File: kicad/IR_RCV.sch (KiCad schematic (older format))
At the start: 19 parts, among them P10 Partition, P5 PR_Host, P6 PR_Slave, P7 Partition, P8 Partition, P9 Partition, Q1 IRFML8244, U6 AD8601

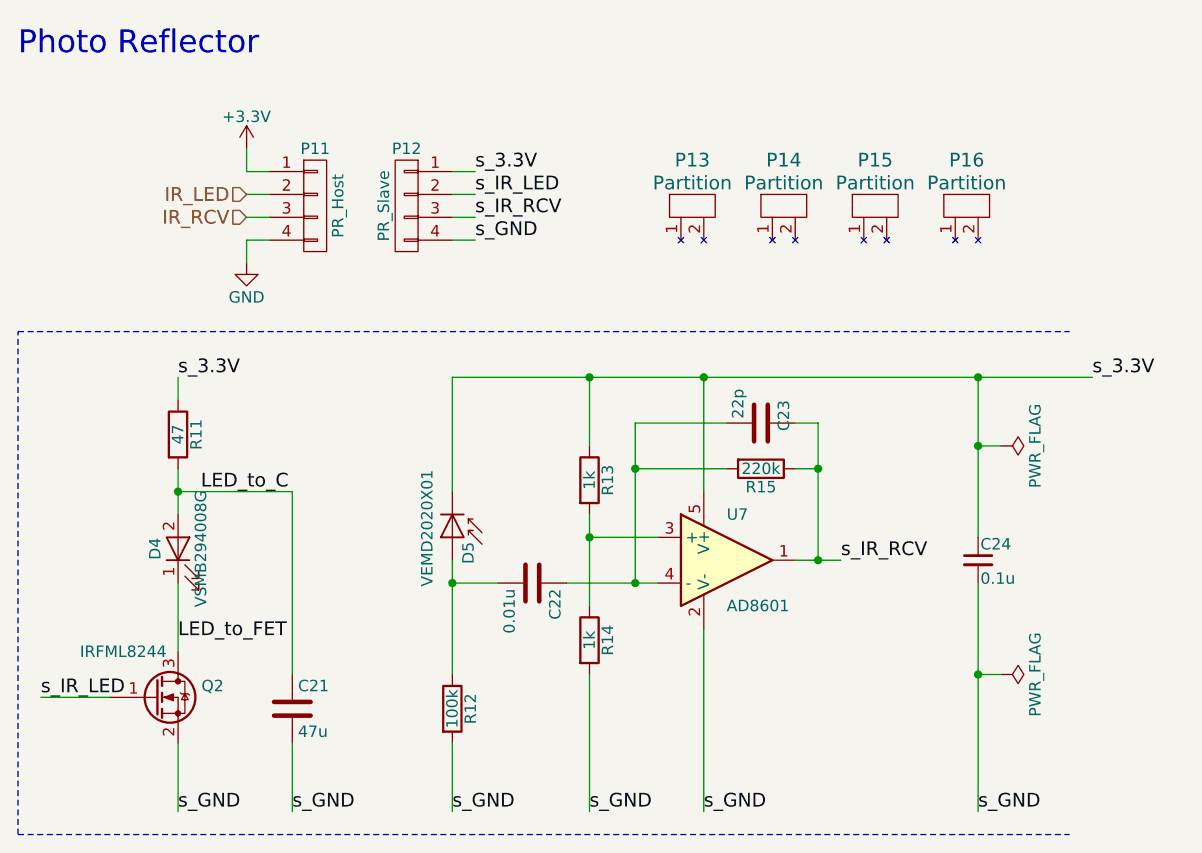
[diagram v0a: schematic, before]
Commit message: 4輪の改良版を設計
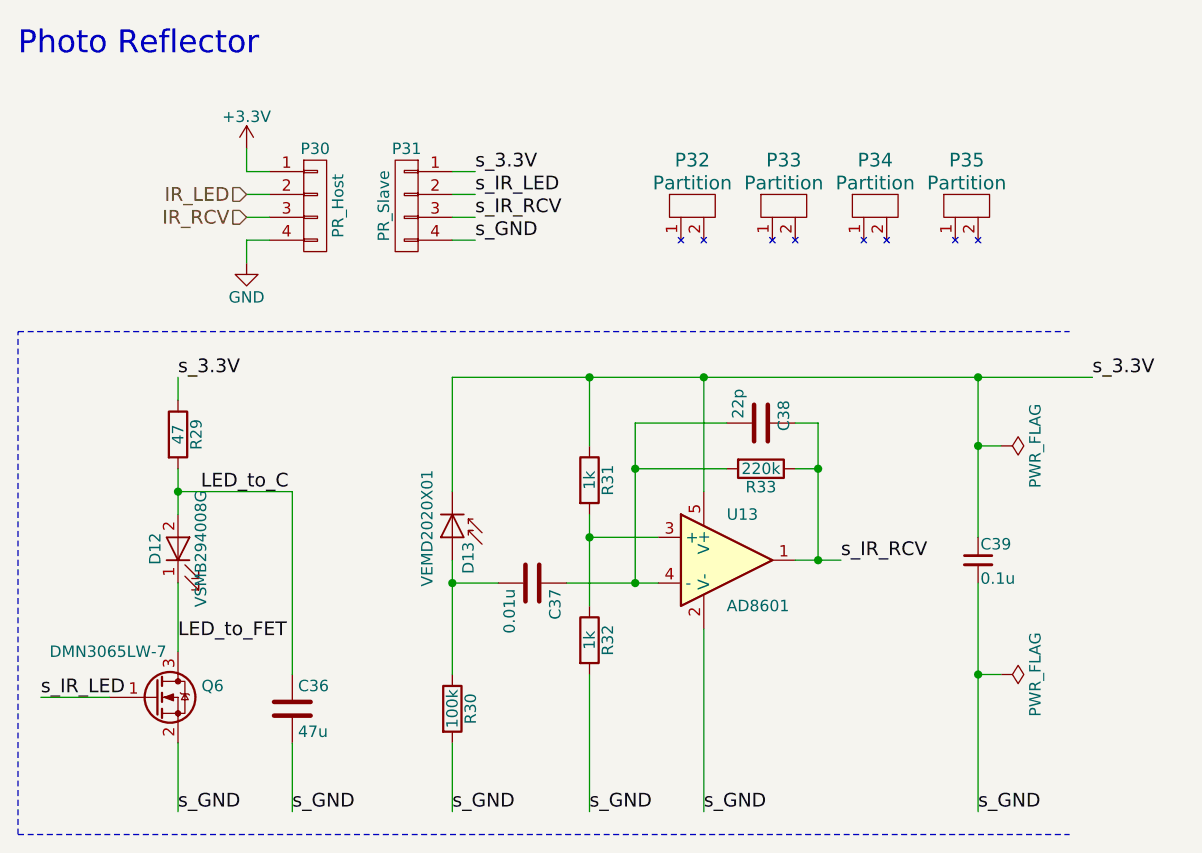
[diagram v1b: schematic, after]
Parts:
- P10: footprint mouse:Partition_Slave -> mouse:Partition_long_Slave
- P9: footprint mouse:Partition_Host -> mouse:Partition_Long_Host
- Q1: value IRFML8244 -> DMN3065LW-7; footprint TO_SOT_Packages_SMD:SOT-23 -> TO_SOT_Packages_SMD:SOT-323_SC-70
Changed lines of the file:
@@
 LIBS:zetex
 LIBS:Zilog
-LIBS:KERISE-cache
 EELAYER 25 0
 EELAYER END
 $Descr A4 11693 8268
 encoding utf-8
-Sheet 5 13
+Sheet 4 14
 Title ""
 Date ""
@@
 AR Path="/57CF0B09/589BE652" Ref="P6"  Part="1"
 AR Path="/57CF2A30/589BE652" Ref="P12"  Part="1"
-F 0 "P12" H 5400 2800 50  0000 C CNN
+AR Path="/597E1B35/589BE652" Ref="P25"  Part="1"
+AR Path="/597E1B39/589BE652" Ref="P31"  Part="1"
+F 0 "P31" H 5400 2800 50  0000 C CNN
 F 1 "PR_Slave" V 5500 2550 50  0000 C CNN
 F 2 "mouse:STAND_PR_SLAVE" H 5400 2550 50  0001 C CNN
@@
 AR Path="/57CF0B09/589BE75A" Ref="Q1"  Part="1"
 AR Path="/57CF2A30/589BE75A" Ref="Q2"  Part="1"
-F 0 "Q2" H 4600 4750 50  0000 R CNN
-F 1 "IRFML8244" H 4350 4900 50  0000 R CNN
-F 2 "TO_SOT_Packages_SMD:SOT-23" H 4500 4800 50  0001 C CNN
+AR Path="/597E1B35/589BE75A" Ref="Q5"  Part="1"
+AR Path="/597E1B39/589BE75A" Ref="Q6"  Part="1"
+F 0 "Q6" H 4600 4750 50  0000 R CNN
+F 1 "DMN3065LW-7" H 4350 4900 50  0000 R CNN
+F 2 "TO_SOT_Packages_SMD:SOT-323_SC-70" H 4500 4800 50  0001 C CNN
 F 3 "" H 4300 4700 50  0000 C CNN
 	1    4300 4700
@@
 AR Path="/57CF0B09/589BE76D" Ref="R6"  Part="1"
 AR Path="/57CF2A30/589BE76D" Ref="R11"  Part="1"
-F 0 "R11" V 4480 3550 50  0000 C CNN
+AR Path="/597E1B35/589BE76D" Ref="R24"  Part="1"
+AR Path="/597E1B39/589BE76D" Ref="R29"  Part="1"
+F 0 "R29" V 4480 3550 50  0000 C CNN
 F 1 "47" V 4400 3550 50  0000 C CNN
 F 2 "Resistors_SMD:R_0603" V 4330 3550 50  0001 C CNN
@@
 AR Path="/57CF0B09/589BE88F" Ref="P5"  Part="1"
 AR Path="/57CF2A30/589BE88F" Ref="P11"  Part="1"
-F 0 "P11" H 5000 2800 50  0000 C CNN
+AR Path="/597E1B35/589BE88F" Ref="P24"  Part="1"
+AR Path="/597E1B39/589BE88F" Ref="P30"  Part="1"
+F 0 "P30" H 5000 2800 50  0000 C CNN
 F 1 "PR_Host" V 5100 2550 50  0000 C CNN
 F 2 "mouse:STAND_PR_HOST" H 5000 2550 50  0001 C CNN
@@
 AR Path="/57CF0B09/589BEE3B" Ref="R7"  Part="1"
 AR Path="/57CF2A30/589BEE3B" Ref="R12"  Part="1"
-F 0 "R12" V 5680 4750 50  0000 C CNN
+AR Path="/597E1B35/589BEE3B" Ref="R25"  Part="1"
+AR Path="/597E1B39/589BEE3B" Ref="R30"  Part="1"
+F 0 "R30" V 5680 4750 50  0000 C CNN
 F 1 "100k" V 5600 4750 50  0000 C CNN
 F 2 "Resistors_SMD:R_0201" V 5530 4750 50  0001 C CNN
@@
 AR Path="/57CF0B09/589BF265" Ref="#PWR038"  Part="1"
 AR Path="/57CF2A30/589BF265" Ref="#PWR042"  Part="1"
-F 0 "#PWR042" H 4700 2550 50  0001 C CNN
+AR Path="/597E1B35/589BF265" Ref="#PWR074"  Part="1"
+AR Path="/597E1B39/589BF265" Ref="#PWR078"  Part="1"
+F 0 "#PWR078" H 4700 2550 50  0001 C CNN
 F 1 "GND" H 4700 2650 50  0000 C CNN
 F 2 "" H 4700 2800 50  0000 C CNN
@@
 AR Path="/57CF0B09/589EE263" Ref="C17"  Part="1"
 AR Path="/57CF2A30/589EE263" Ref="C21"  Part="1"
-F 0 "C21" H 4925 4850 50  0000 L CNN
+AR Path="/597E1B35/589EE263" Ref="C32"  Part="1"
+AR Path="/597E1B39/589EE263" Ref="C36"  Part="1"
+F 0 "C36" H 4925 4850 50  0000 L CNN
 F 1 "47u" H 4925 4650 50  0000 L CNN
 F 2 "Capacitors_SMD:C_0805" H 4938 4600 50  0001 C CNN
@@
 AR Path="/57CF0B09/589CC209" Ref="#PWR039"  Part="1"
 AR Path="/57CF2A30/589CC209" Ref="#PWR043"  Part="1"
-F 0 "#PWR043" H 4700 2150 50  0001 C CNN
+AR Path="/597E1B35/589CC209" Ref="#PWR075"  Part="1"
+AR Path="/597E1B39/589CC209" Ref="#PWR079"  Part="1"
+F 0 "#PWR079" H 4700 2150 50  0001 C CNN
 F 1 "+3.3V" H 4700 2440 50  0000 C CNN
 F 2 "" H 4700 2300 50  0000 C CNN
@@
 AR Path="/57CF0B09/58A0483E" Ref="R8"  Part="1"
 AR Path="/57CF2A30/58A0483E" Ref="R13"  Part="1"
-F 0 "R13" V 6280 3750 50  0000 C CNN
+AR Path="/597E1B35/58A0483E" Ref="R26"  Part="1"
+AR Path="/597E1B39/58A0483E" Ref="R31"  Part="1"
+F 0 "R31" V 6280 3750 50  0000 C CNN
 F 1 "1k" V 6200 3750 50  0000 C CNN
 F 2 "Resistors_SMD:R_0201" V 6130 3750 50  0001 C CNN
@@
 AR Path="/57CF0B09/57CF0F5E" Ref="C19"  Part="1"
 AR Path="/57CF2A30/57CF0F5E" Ref="C23"  Part="1"
-F 0 "C23" H 6850 3600 50  0000 L CNN
+AR Path="/597E1B35/57CF0F5E" Ref="C34"  Part="1"
+AR Path="/597E1B39/57CF0F5E" Ref="C38"  Part="1"
+F 0 "C38" H 6850 3600 50  0000 L CNN
 F 1 "22p" H 6800 3400 50  0000 L CNN
 F 2 "Capacitors_SMD:C_0201" H 6988 3350 50  0001 C CNN
@@
 AR Path="/57CF0B09/57CF0F57" Ref="R10"  Part="1"
 AR Path="/57CF2A30/57CF0F57" Ref="R15"  Part="1"
-F 0 "R15" V 7030 3700 50  0000 C CNN
+AR Path="/597E1B35/57CF0F57" Ref="R28"  Part="1"
+AR Path="/597E1B39/57CF0F57" Ref="R33"  Part="1"
+F 0 "R33" V 7030 3700 50  0000 C CNN
 F 1 "220k" V 6950 3700 50  0000 C CNN
 F 2 "Resistors_SMD:R_0201" V 6880 3700 50  0001 C CNN
@@
 AR Path="/57CF0B09/5925867D" Ref="C20"  Part="1"
 AR Path="/57CF2A30/5925867D" Ref="C24"  Part="1"
-F 0 "C24" H 7910 4170 50  0000 L CNN
+AR Path="/597E1B35/5925867D" Ref="C35"  Part="1"
+AR Path="/597E1B39/5925867D" Ref="C39"  Part="1"
+F 0 "C39" H 7910 4170 50  0000 L CNN
 F 1 "0.1u" H 7910 4020 50  0000 L CNN
 F 2 "Capacitors_SMD:C_0201" H 7900 4100 50  0001 C CNN
@@
 AR Path="/57CF0B09/58A04889" Ref="R9"  Part="1"
 AR Path="/57CF2A30/58A04889" Ref="R14"  Part="1"
-F 0 "R14" V 6280 4450 50  0000 C CNN
+AR Path="/597E1B35/58A04889" Ref="R27"  Part="1"
+AR Path="/597E1B39/58A04889" Ref="R32"  Part="1"
+F 0 "R32" V 6280 4450 50  0000 C CNN
 F 1 "1k" V 6200 4450 50  0000 C CNN
 F 2 "Resistors_SMD:R_0201" V 6130 4450 50  0001 C CNN
@@
 AR Path="/57CF0B09/57CF0F45" Ref="C18"  Part="1"
 AR Path="/57CF2A30/57CF0F45" Ref="C22"  Part="1"
-F 0 "C22" H 5975 4300 50  0000 L CNN
+AR Path="/597E1B35/57CF0F45" Ref="C33"  Part="1"
+AR Path="/597E1B39/57CF0F45" Ref="C37"  Part="1"
+F 0 "C37" H 5975 4300 50  0000 L CNN
 F 1 "0.01u" H 5975 4100 50  0000 L CNN
 F 2 "Capacitors_SMD:C_0201" H 5988 4050 50  0001 C CNN
@@
 AR Path="/57CF0B09/59497B18" Ref="P7"  Part="1"
 AR Path="/57CF2A30/59497B18" Ref="P13"  Part="1"
-F 0 "P13" H 6650 2550 60  0000 C CNN
+AR Path="/597E1B35/59497B18" Ref="P26"  Part="1"
+AR Path="/597E1B39/59497B18" Ref="P32"  Part="1"
+F 0 "P32" H 6650 2550 60  0000 C CNN
 F 1 "Partition" H 6650 2450 60  0000 C CNN
 F 2 "mouse:Partition_Host" H 6650 2450 60  0001 C CNN
@@
 AR Path="/57CF0B09/59497CA2" Ref="P8"  Part="1"
 AR Path="/57CF2A30/59497CA2" Ref="P14"  Part="1"
-F 0 "P14" H 7050 2550 60  0000 C CNN
+AR Path="/597E1B35/59497CA2" Ref="P27"  Part="1"
+AR Path="/597E1B39/59497CA2" Ref="P33"  Part="1"
+F 0 "P33" H 7050 2550 60  0000 C CNN
 F 1 "Partition" H 7050 2450 60  0000 C CNN
 F 2 "mouse:Partition_Slave" H 7050 2450 60  0001 C CNN
@@
 AR Path="/57CF0B09/59497CF1" Ref="P9"  Part="1"
 AR Path="/57CF2A30/59497CF1" Ref="P15"  Part="1"
-F 0 "P15" H 7450 2550 60  0000 C CNN
+AR Path="/597E1B35/59497CF1" Ref="P28"  Part="1"
+AR Path="/597E1B39/59497CF1" Ref="P34"  Part="1"
+F 0 "P34" H 7450 2550 60  0000 C CNN
 F 1 "Partition" H 7450 2450 60  0000 C CNN
-F 2 "mouse:Partition_Host" H 7450 2450 60  0001 C CNN
+F 2 "mouse:Partition_Long_Host" H 7450 2450 60  0001 C CNN
 F 3 "" H 7450 2450 60  0001 C CNN
 	1    7450 2450
@@
 AR Path="/57CF0B09/59497D43" Ref="P10"  Part="1"
 AR Path="/57CF2A30/59497D43" Ref="P16"  Part="1"
-F 0 "P16" H 7850 2550 60  0000 C CNN
+AR Path="/597E1B35/59497D43" Ref="P29"  Part="1"
+AR Path="/597E1B39/59497D43" Ref="P35"  Part="1"
+F 0 "P35" H 7850 2550 60  0000 C CNN
 F 1 "Partition" H 7850 2450 60  0000 C CNN
-F 2 "mouse:Partition_Slave" H 7850 2450 60  0001 C CNN
+F 2 "mouse:Partition_long_Slave" H 7850 2450 60  0001 C CNN
 F 3 "" H 7850 2450 60  0001 C CNN
 	1    7850 2450
@@
 AR Path="/57CF0B09/594AC13D" Ref="U6"  Part="1"
 AR Path="/57CF2A30/594AC13D" Ref="U7"  Part="1"
-F 0 "U7" H 6800 4300 50  0000 L CNN
+AR Path="/597E1B35/594AC13D" Ref="U12"  Part="1"
+AR Path="/597E1B39/594AC13D" Ref="U13"  Part="1"
+F 0 "U13" H 6800 4300 50  0000 L CNN
 F 1 "AD8601" H 6800 3900 50  0000 L CNN
 F 2 "TO_SOT_Packages_SMD:SOT-23-5" H 6800 3700 50  0001 C CNN
@@
 AR Path="/57CF0B09/594AC36C" Ref="D3"  Part="1"
 AR Path="/57CF2A30/594AC36C" Ref="D5"  Part="1"
-F 0 "D5" H 5620 4070 50  0000 L CNN
+AR Path="/597E1B35/594AC36C" Ref="D11"  Part="1"
+AR Path="/597E1B39/594AC36C" Ref="D13"  Part="1"
+F 0 "D13" H 5620 4070 50  0000 L CNN
 F 1 "VEMD2020X01" H 5560 3890 50  0000 C CNN
 F 2 "mouse:VISHAY_DIODE" H 5550 4000 50  0001 C CNN
@@
 AR Path="/57CF0B09/594AC674" Ref="D2"  Part="1"
 AR Path="/57CF2A30/594AC674" Ref="D4"  Part="1"
-F 0 "D4" H 4400 4150 50  0000 C CNN
+AR Path="/597E1B35/594AC674" Ref="D10"  Part="1"
+AR Path="/597E1B39/594AC674" Ref="D12"  Part="1"
+F 0 "D12" H 4400 4150 50  0000 C CNN
 F 1 "VSMB294008G" H 4400 3950 50  0000 C CNN
 F 2 "mouse:VISHAY_DIODE" H 4400 4050 50  0001 C CNN
@@
 AR Path="/57CF0B09/594B7401" Ref="#FLG040"  Part="1"
 AR Path="/57CF2A30/594B7401" Ref="#FLG044"  Part="1"
-F 0 "#FLG044" H 8000 3675 50  0001 C CNN
+AR Path="/597E1B35/594B7401" Ref="#FLG076"  Part="1"
+AR Path="/597E1B39/594B7401" Ref="#FLG080"  Part="1"
+F 0 "#FLG080" H 8000 3675 50  0001 C CNN
 F 1 "PWR_FLAG" H 8000 3750 50  0000 C CNN
 F 2 "" H 8000 3600 50  0001 C CNN
@@
 AR Path="/57CF0B09/594B744C" Ref="#FLG041"  Part="1"
 AR Path="/57CF2A30/594B744C" Ref="#FLG045"  Part="1"
-F 0 "#FLG045" H 8000 4675 50  0001 C CNN
+AR Path="/597E1B35/594B744C" Ref="#FLG077"  Part="1"
+AR Path="/597E1B39/594B744C" Ref="#FLG081"  Part="1"
+F 0 "#FLG081" H 8000 4675 50  0001 C CNN
 F 1 "PWR_FLAG" H 8000 4750 50  0000 C CNN
 F 2 "" H 8000 4600 50  0001 C CNN

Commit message: 部品を配置
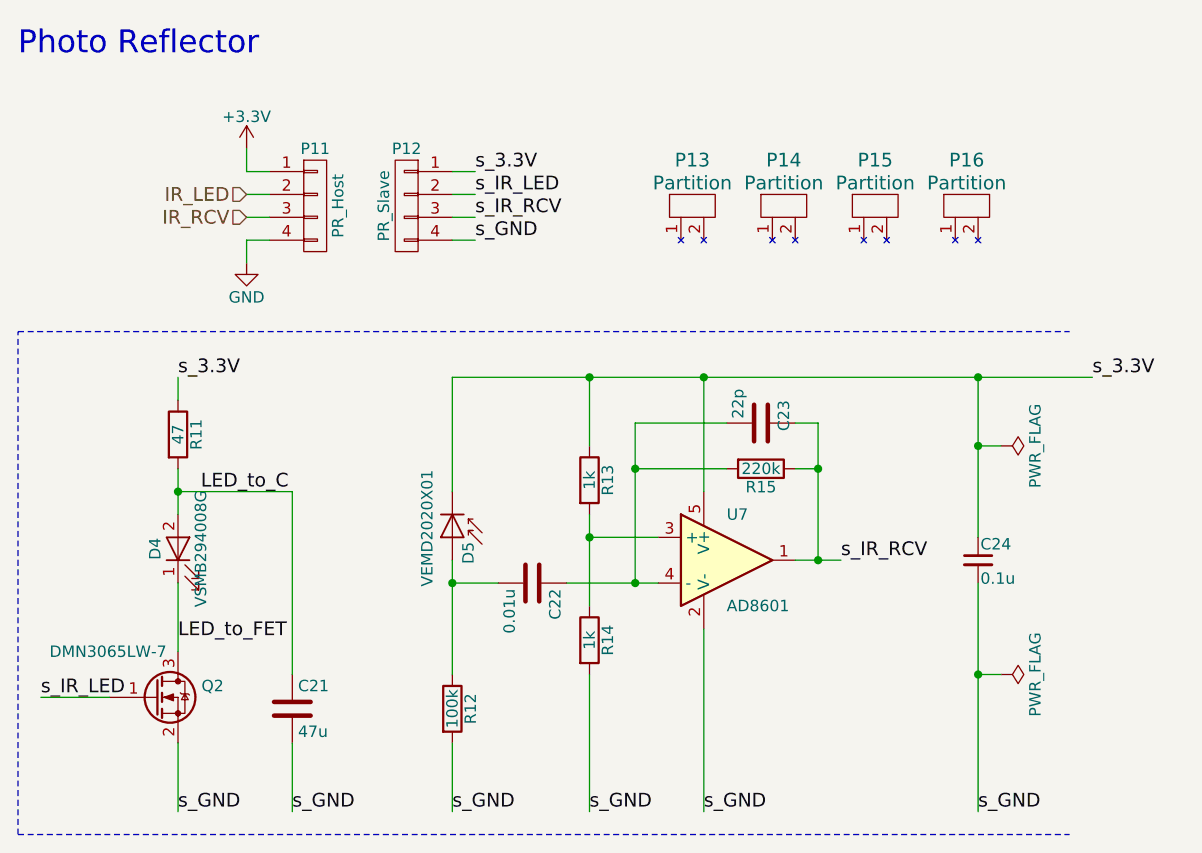
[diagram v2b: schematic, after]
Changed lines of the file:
@@
 AR Path="/597E1B35/589BE652" Ref="P25"  Part="1"
 AR Path="/597E1B39/589BE652" Ref="P31"  Part="1"
-F 0 "P31" H 5400 2800 50  0000 C CNN
+F 0 "P12" H 5400 2800 50  0000 C CNN
 F 1 "PR_Slave" V 5500 2550 50  0000 C CNN
 F 2 "mouse:STAND_PR_SLAVE" H 5400 2550 50  0001 C CNN
@@
 AR Path="/597E1B35/589BE75A" Ref="Q5"  Part="1"
 AR Path="/597E1B39/589BE75A" Ref="Q6"  Part="1"
-F 0 "Q6" H 4600 4750 50  0000 R CNN
+F 0 "Q2" H 4600 4750 50  0000 R CNN
 F 1 "DMN3065LW-7" H 4350 4900 50  0000 R CNN
 F 2 "TO_SOT_Packages_SMD:SOT-323_SC-70" H 4500 4800 50  0001 C CNN
@@
 AR Path="/597E1B35/589BE76D" Ref="R24"  Part="1"
 AR Path="/597E1B39/589BE76D" Ref="R29"  Part="1"
-F 0 "R29" V 4480 3550 50  0000 C CNN
+F 0 "R11" V 4480 3550 50  0000 C CNN
 F 1 "47" V 4400 3550 50  0000 C CNN
 F 2 "Resistors_SMD:R_0603" V 4330 3550 50  0001 C CNN
@@
 AR Path="/597E1B35/589BE88F" Ref="P24"  Part="1"
 AR Path="/597E1B39/589BE88F" Ref="P30"  Part="1"
-F 0 "P30" H 5000 2800 50  0000 C CNN
+F 0 "P11" H 5000 2800 50  0000 C CNN
 F 1 "PR_Host" V 5100 2550 50  0000 C CNN
 F 2 "mouse:STAND_PR_HOST" H 5000 2550 50  0001 C CNN
@@
 AR Path="/597E1B35/589BEE3B" Ref="R25"  Part="1"
 AR Path="/597E1B39/589BEE3B" Ref="R30"  Part="1"
-F 0 "R30" V 5680 4750 50  0000 C CNN
+F 0 "R12" V 5680 4750 50  0000 C CNN
 F 1 "100k" V 5600 4750 50  0000 C CNN
 F 2 "Resistors_SMD:R_0201" V 5530 4750 50  0001 C CNN
@@
 AR Path="/597E1B35/589EE263" Ref="C32"  Part="1"
 AR Path="/597E1B39/589EE263" Ref="C36"  Part="1"
-F 0 "C36" H 4925 4850 50  0000 L CNN
+F 0 "C21" H 4925 4850 50  0000 L CNN
 F 1 "47u" H 4925 4650 50  0000 L CNN
 F 2 "Capacitors_SMD:C_0805" H 4938 4600 50  0001 C CNN
@@
 AR Path="/597E1B35/58A0483E" Ref="R26"  Part="1"
 AR Path="/597E1B39/58A0483E" Ref="R31"  Part="1"
-F 0 "R31" V 6280 3750 50  0000 C CNN
+F 0 "R13" V 6280 3750 50  0000 C CNN
 F 1 "1k" V 6200 3750 50  0000 C CNN
 F 2 "Resistors_SMD:R_0201" V 6130 3750 50  0001 C CNN
@@
 AR Path="/597E1B35/57CF0F5E" Ref="C34"  Part="1"
 AR Path="/597E1B39/57CF0F5E" Ref="C38"  Part="1"
-F 0 "C38" H 6850 3600 50  0000 L CNN
+F 0 "C23" H 6850 3600 50  0000 L CNN
 F 1 "22p" H 6800 3400 50  0000 L CNN
 F 2 "Capacitors_SMD:C_0201" H 6988 3350 50  0001 C CNN
@@
 AR Path="/597E1B35/57CF0F57" Ref="R28"  Part="1"
 AR Path="/597E1B39/57CF0F57" Ref="R33"  Part="1"
-F 0 "R33" V 7030 3700 50  0000 C CNN
+F 0 "R15" V 7030 3700 50  0000 C CNN
 F 1 "220k" V 6950 3700 50  0000 C CNN
 F 2 "Resistors_SMD:R_0201" V 6880 3700 50  0001 C CNN
@@
 AR Path="/597E1B35/5925867D" Ref="C35"  Part="1"
 AR Path="/597E1B39/5925867D" Ref="C39"  Part="1"
-F 0 "C39" H 7910 4170 50  0000 L CNN
+F 0 "C24" H 7910 4170 50  0000 L CNN
 F 1 "0.1u" H 7910 4020 50  0000 L CNN
 F 2 "Capacitors_SMD:C_0201" H 7900 4100 50  0001 C CNN
@@
 AR Path="/597E1B35/58A04889" Ref="R27"  Part="1"
 AR Path="/597E1B39/58A04889" Ref="R32"  Part="1"
-F 0 "R32" V 6280 4450 50  0000 C CNN
+F 0 "R14" V 6280 4450 50  0000 C CNN
 F 1 "1k" V 6200 4450 50  0000 C CNN
 F 2 "Resistors_SMD:R_0201" V 6130 4450 50  0001 C CNN
@@
 AR Path="/597E1B35/57CF0F45" Ref="C33"  Part="1"
 AR Path="/597E1B39/57CF0F45" Ref="C37"  Part="1"
-F 0 "C37" H 5975 4300 50  0000 L CNN
+F 0 "C22" H 5975 4300 50  0000 L CNN
 F 1 "0.01u" H 5975 4100 50  0000 L CNN
 F 2 "Capacitors_SMD:C_0201" H 5988 4050 50  0001 C CNN
@@
 AR Path="/597E1B35/59497B18" Ref="P26"  Part="1"
 AR Path="/597E1B39/59497B18" Ref="P32"  Part="1"
-F 0 "P32" H 6650 2550 60  0000 C CNN
+F 0 "P13" H 6650 2550 60  0000 C CNN
 F 1 "Partition" H 6650 2450 60  0000 C CNN
 F 2 "mouse:Partition_Host" H 6650 2450 60  0001 C CNN
@@
 AR Path="/597E1B35/59497CA2" Ref="P27"  Part="1"
 AR Path="/597E1B39/59497CA2" Ref="P33"  Part="1"
-F 0 "P33" H 7050 2550 60  0000 C CNN
+F 0 "P14" H 7050 2550 60  0000 C CNN
 F 1 "Partition" H 7050 2450 60  0000 C CNN
 F 2 "mouse:Partition_Slave" H 7050 2450 60  0001 C CNN
@@
 AR Path="/597E1B35/59497CF1" Ref="P28"  Part="1"
 AR Path="/597E1B39/59497CF1" Ref="P34"  Part="1"
-F 0 "P34" H 7450 2550 60  0000 C CNN
+F 0 "P15" H 7450 2550 60  0000 C CNN
 F 1 "Partition" H 7450 2450 60  0000 C CNN
 F 2 "mouse:Partition_Long_Host" H 7450 2450 60  0001 C CNN
@@
 AR Path="/597E1B35/59497D43" Ref="P29"  Part="1"
 AR Path="/597E1B39/59497D43" Ref="P35"  Part="1"
-F 0 "P35" H 7850 2550 60  0000 C CNN
+F 0 "P16" H 7850 2550 60  0000 C CNN
 F 1 "Partition" H 7850 2450 60  0000 C CNN
 F 2 "mouse:Partition_long_Slave" H 7850 2450 60  0001 C CNN
@@
 AR Path="/597E1B35/594AC13D" Ref="U12"  Part="1"
 AR Path="/597E1B39/594AC13D" Ref="U13"  Part="1"
-F 0 "U13" H 6800 4300 50  0000 L CNN
+F 0 "U7" H 6800 4300 50  0000 L CNN
 F 1 "AD8601" H 6800 3900 50  0000 L CNN
 F 2 "TO_SOT_Packages_SMD:SOT-23-5" H 6800 3700 50  0001 C CNN
@@
 AR Path="/597E1B35/594AC36C" Ref="D11"  Part="1"
 AR Path="/597E1B39/594AC36C" Ref="D13"  Part="1"
-F 0 "D13" H 5620 4070 50  0000 L CNN
+F 0 "D5" H 5620 4070 50  0000 L CNN
 F 1 "VEMD2020X01" H 5560 3890 50  0000 C CNN
 F 2 "mouse:VISHAY_DIODE" H 5550 4000 50  0001 C CNN
@@
 AR Path="/597E1B35/594AC674" Ref="D10"  Part="1"
 AR Path="/597E1B39/594AC674" Ref="D12"  Part="1"
-F 0 "D12" H 4400 4150 50  0000 C CNN
+F 0 "D4" H 4400 4150 50  0000 C CNN
 F 1 "VSMB294008G" H 4400 3950 50  0000 C CNN
 F 2 "mouse:VISHAY_DIODE" H 4400 4050 50  0001 C CNN
